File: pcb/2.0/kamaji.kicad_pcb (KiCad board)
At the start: 2 copper layers, 100 x 100 mm, 82 parts, among them J1 RJ10, J2 RJ10, J3 RJ10, J4 RJ10, J5 RJ10, J6 RJ10, J7 USB_B, J8 USB_A, Q1 2N3904, Q2 IRL540N, Q3 IRL540N, SW1 SW_Push, SW2 SW_Push, SW3 SW_Push, U1 ATMEGA32U4-AU, Y1 16MHz

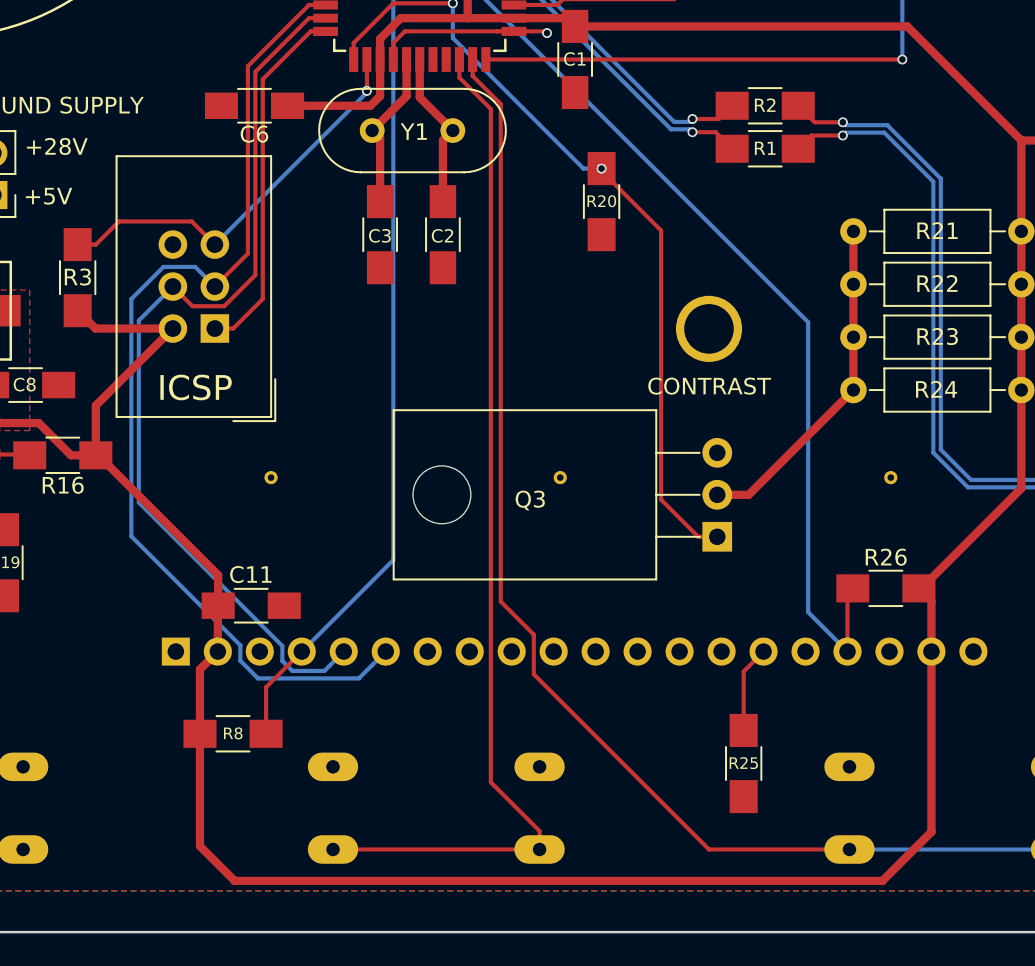
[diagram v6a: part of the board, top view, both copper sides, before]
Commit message: pull LCD_CS down
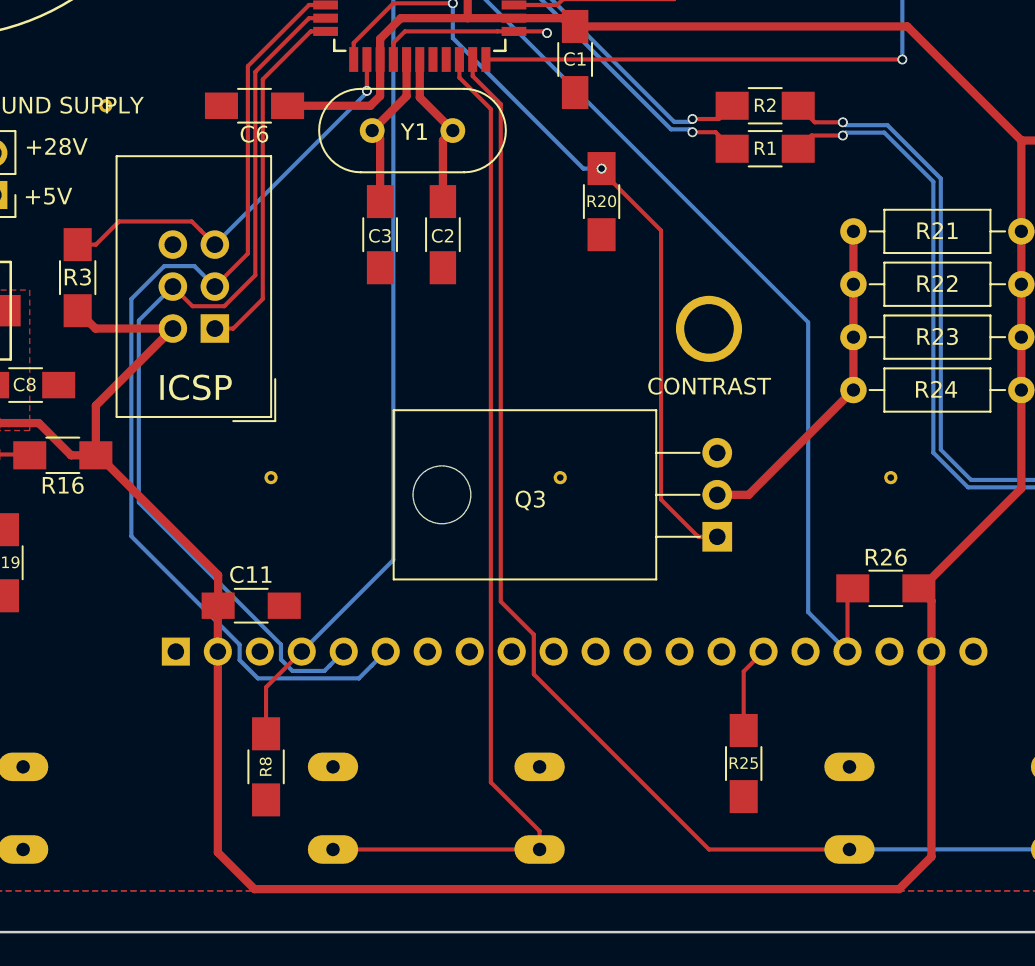
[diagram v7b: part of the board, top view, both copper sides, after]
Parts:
- added VIA**: Via_0.8mm, kamaji:Via_0.8mm, F.Cu at (80.0, 100.0)
- moved R8 2.83 mm to (89.7, 140.0), turned to 90 degrees
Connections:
- R8 pad 1: VCC -> GND
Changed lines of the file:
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@@
 (kicad_pcb (version 4) (host pcbnew 4.0.7)
   (general
-    (links 0)
-    (no_connects 0)
+    (links 178)
+    (no_connects 2)
     (area 49.924999 49.924999 150.075001 150.075001)
     (thickness 1.6)
     (drawings 16)
-    (tracks 380)
+    (tracks 378)
     (zones 0)
-    (modules 82)
+    (modules 83)
     (nets 57)
   )
@@
     (add_net VCC)
   )
+  (module kamaji:Via_0.8mm (layer F.Cu)
+    (at 80 100)
+    (fp_text reference VIA** (at 0 1.5) (layer F.SilkS) hide
+      (effects (font (size 1 1) (thickness 0.15)))
+    )
+    (fp_text value Via_0.8mm (at 0 -1.5) (layer F.Fab) hide
+      (effects (font (size 1 1) (thickness 0.15)))
+    )
+    (pad 1 thru_hole circle (at 0 0) (size 0.8 0.8) (drill 0.4) (layers *.Cu *.Mask)
+      (net 49 GND) (zone_connect 2))
+  )
   (module Connectors:1pin (layer F.Cu)
     (at 54 57)
@@
   )
   (module Resistors_SMD:R_1206_HandSoldering (layer F.Cu)
-    (at 87.7 138)
+    (at 89.7 140 90)
     (descr "Resistor SMD 1206, hand soldering")
     (tags "resistor 1206")
     (attr smd)
-    (fp_text reference R8 (at 0 0) (layer F.SilkS)
+    (fp_text reference R8 (at 0 0 90) (layer F.SilkS)
       (effects (font (size 0.7 0.7) (thickness 0.15)))
     )
-    (fp_text value 10K (at 0 1.9) (layer F.Fab)
-      (effects (font (size 1 1) (thickness 0.15)))
-    )
-    (fp_text user %R (at 0 0) (layer F.Fab)
+    (fp_text value 10K (at 0 1.9 90) (layer F.Fab)
+      (effects (font (size 1 1) (thickness 0.15)))
+    )
+    (fp_text user %R (at 0 0 90) (layer F.Fab)
       (effects (font (size 0.7 0.7) (thickness 0.105)))
     )
@@
     (fp_line (start 3.25 1.1) (end 3.25 -1.11) (layer F.CrtYd) (width 0.05))
     (fp_line (start 3.25 1.1) (end -3.25 1.1) (layer F.CrtYd) (width 0.05))
-    (pad 1 smd rect (at -2 0) (size 2 1.7) (layers F.Cu F.Paste F.Mask)
-      (net 3 VCC))
-    (pad 2 smd rect (at 2 0) (size 2 1.7) (layers F.Cu F.Paste F.Mask)
+    (pad 1 smd rect (at -2 0 90) (size 2 1.7) (layers F.Cu F.Paste F.Mask)
+      (net 49 GND))
+    (pad 2 smd rect (at 2 0 90) (size 2 1.7) (layers F.Cu F.Paste F.Mask)
       (net 7 /LCD_CS))
     (model ${KISYS3DMOD}/Resistors_SMD.3dshapes/R_1206.wrl
@@
   (segment (start 72.85 121.1) (end 75.35 121.1) (width 0.25) (layer F.Cu) (net 2))
   (segment (start 75.35 121.1) (end 75.4 121.15) (width 0.25) (layer F.Cu) (net 2))
+  (segment (start 129.961034 133.024284) (end 129.961034 145.438966) (width 0.5) (layer F.Cu) (net 3))
+  (segment (start 129.961034 145.438966) (end 128 147.4) (width 0.5) (layer F.Cu) (net 3))
+  (segment (start 89 147.4) (end 86.781034 145.181034) (width 0.5) (layer F.Cu) (net 3))
+  (segment (start 128 147.4) (end 89 147.4) (width 0.5) (layer F.Cu) (net 3))
+  (segment (start 86.781034 145.181034) (end 86.781034 133.024284) (width 0.5) (layer F.Cu) (net 3))
   (segment (start 96.6 88.05) (end 96.6 85.8) (width 0.5) (layer F.Cu) (net 3))
   (segment (start 96.6 88.05) (end 96.6 89.7) (width 0.5) (layer F.Cu) (net 3))
-  (segment (start 129.961034 133.024284) (end 129.961034 143.938966) (width 0.5) (layer F.Cu) (net 3))
-  (segment (start 129.961034 143.938966) (end 127 146.9) (width 0.5) (layer F.Cu) (net 3))
-  (segment (start 127 146.9) (end 87.8 146.9) (width 0.5) (layer F.Cu) (net 3))
-  (segment (start 85.7 144.8) (end 85.7 138) (width 0.5) (layer F.Cu) (net 3))
-  (segment (start 87.8 146.9) (end 85.7 144.8) (width 0.5) (layer F.Cu) (net 3))
   (segment (start 93.3 92.3) (end 94.55 92.3) (width 0.5) (layer F.Cu) (net 3))
   (segment (start 94.55 92.3) (end 96.6 90.25) (width 0.5) (layer F.Cu) (net 3))
@@
   (segment (start 86.781034 133.024284) (end 86.781034 130.268966) (width 0.5) (layer F.Cu) (net 3))
   (segment (start 86.781034 130.268966) (end 86.8 130.25) (width 0.5) (layer F.Cu) (net 3))
-  (segment (start 85.7 138) (end 85.7 134.105318) (width 0.5) (layer F.Cu) (net 3))
-  (segment (start 85.7 134.105318) (end 86.781034 133.024284) (width 0.5) (layer F.Cu) (net 3))
   (segment (start 135.4 117.2) (end 135.4 123.15) (width 0.5) (layer F.Cu) (net 3))
   (segment (start 129.35 129.2) (end 129.2 129.2) (width 0.5) (layer F.Cu) (net 3))
@@
   (segment (start 91.861034 133.024284) (end 89.7 135.185318) (width 0.25) (layer F.Cu) (net 7))
   (segment (start 89.7 135.185318) (end 89.7 138) (width 0.25) (layer F.Cu) (net 7))
+  (segment (start 84.06 110.94) (end 82.000022 112.999978) (width 0.25) (layer B.Cu) (net 8))
+  (segment (start 82.000022 112.999978) (end 82.000022 124.000022) (width 0.25) (layer B.Cu) (net 8))
+  (segment (start 82.000022 124.000022) (end 90.6 132.6) (width 0.25) (layer B.Cu) (net 8))
+  (segment (start 90.6 132.6) (end 90.6 133.502252) (width 0.25) (layer B.Cu) (net 8))
+  (segment (start 90.6 133.502252) (end 91.297032 134.199284) (width 0.25) (layer B.Cu) (net 8))
+  (segment (start 91.297032 134.199284) (end 93.226034 134.199284) (width 0.25) (layer B.Cu) (net 8))
+  (segment (start 93.226034 134.199284) (end 93.551035 133.874283) (width 0.25) (layer B.Cu) (net 8))
   (segment (start 93.551035 133.874283) (end 94.401034 133.024284) (width 0.25) (layer B.Cu) (net 8))
-  (segment (start 93.226034 134.199284) (end 93.551035 133.874283) (width 0.25) (layer B.Cu) (net 8))
-  (segment (start 90.686033 132.686033) (end 90.686033 133.588285) (width 0.25) (layer B.Cu) (net 8))
-  (segment (start 90.686033 133.588285) (end 91.297032 134.199284) (width 0.25) (layer B.Cu) (net 8))
-  (segment (start 91.297032 134.199284) (end 93.226034 134.199284) (width 0.25) (layer B.Cu) (net 8))
-  (segment (start 84.06 110.94) (end 82.000022 112.999978) (width 0.25) (layer B.Cu) (net 8))
-  (segment (start 82.000022 124.000022) (end 90.686033 132.686033) (width 0.25) (layer B.Cu) (net 8))
-  (segment (start 82.000022 112.999978) (end 82.000022 124.000022) (width 0.25) (layer B.Cu) (net 8))
   (segment (start 87.170529 112.128601) (end 89.049989 110.249141) (width 0.25) (layer F.Cu) (net 8))
   (segment (start 85.248601 112.128601) (end 87.170529 112.128601) (width 0.25) (layer F.Cu) (net 8))
@@
   (segment (start 89.049989 97.950011) (end 92.3 94.7) (width 0.25) (layer F.Cu) (net 8))
   (segment (start 89.049989 110.249141) (end 89.049989 97.950011) (width 0.25) (layer F.Cu) (net 8))
+  (segment (start 86.6 110.94) (end 85.36 109.7) (width 0.25) (layer B.Cu) (net 9))
+  (segment (start 85.36 109.7) (end 83.54087 109.7) (width 0.25) (layer B.Cu) (net 9))
+  (segment (start 81.550011 111.690859) (end 81.550011 126.054259) (width 0.25) (layer B.Cu) (net 9))
+  (segment (start 81.550011 126.054259) (end 88.1 132.604248) (width 0.25) (layer B.Cu) (net 9))
+  (segment (start 88.1 133.542252) (end 89.207043 134.649295) (width 0.25) (layer B.Cu) (net 9))
+  (segment (start 89.207043 134.649295) (end 95.316023 134.649295) (width 0.25) (layer B.Cu) (net 9))
   (segment (start 96.091035 133.874283) (end 96.941034 133.024284) (width 0.25) (layer B.Cu) (net 9))
-  (segment (start 88.146033 133.588285) (end 89.207043 134.649295) (width 0.25) (layer B.Cu) (net 9))
-  (segment (start 83.489471 109.751399) (end 81.550011 111.690859) (width 0.25) (layer B.Cu) (net 9))
-  (segment (start 88.146033 132.650281) (end 88.146033 133.588285) (width 0.25) (layer B.Cu) (net 9))
-  (segment (start 81.550011 111.690859) (end 81.550011 126.054259) (width 0.25) (layer B.Cu) (net 9))
-  (segment (start 81.550011 126.054259) (end 88.146033 132.650281) (width 0.25) (layer B.Cu) (net 9))
-  (segment (start 89.207043 134.649295) (end 95.316023 134.649295) (width 0.25) (layer B.Cu) (net 9))
+  (segment (start 83.54087 109.7) (end 81.550011 111.690859) (width 0.25) (layer B.Cu) (net 9))
+  (segment (start 88.1 132.604248) (end 88.1 133.542252) (width 0.25) (layer B.Cu) (net 9))
   (segment (start 95.316023 134.649295) (end 96.091035 133.874283) (width 0.25) (layer B.Cu) (net 9))
-  (segment (start 85.411399 109.751399) (end 83.489471 109.751399) (width 0.25) (layer B.Cu) (net 9))
-  (segment (start 86.6 110.94) (end 85.411399 109.751399) (width 0.25) (layer B.Cu) (net 9))
   (segment (start 92.3 93.9) (end 93.3 93.9) (width 0.25) (layer F.Cu) (net 9))
   (segment (start 88.599978 97.600022) (end 92.3 93.9) (width 0.25) (layer F.Cu) (net 9))

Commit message: minor PCB changes
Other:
- board text added: "SOUND"
- board text removed: "SOUND SUPPLY"
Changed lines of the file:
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@@
   (general
     (links 178)
-    (no_connects 2)
-    (area 49.924999 49.924999 150.075001 150.075001)
+    (no_connects 0)
+    (area 46.224999 46.55 157.775001 150.075001)
     (thickness 1.6)
     (drawings 16)
@@
     (pad_drill 3.048)
     (pad_to_mask_clearance 0.2)
-    (aux_axis_origin 0 0)
+    (aux_axis_origin 50 50)
     (visible_elements FFFFEF7F)
     (pcbplotparams
-      (layerselection 0x00030_80000001)
-      (usegerberextensions false)
+      (layerselection 0x010f0_80000001)
+      (usegerberextensions true)
       (excludeedgelayer true)
       (linewidth 0.100000)
@@
       (viasonmask false)
       (mode 1)
-      (useauxorigin false)
+      (useauxorigin true)
       (hpglpennumber 1)
       (hpglpenspeed 20)
@@
       (plotinvisibletext false)
       (padsonsilk false)
-      (subtractmaskfromsilk false)
+      (subtractmaskfromsilk true)
       (outputformat 1)
       (mirror false)
-      (drillshape 1)
+      (drillshape 0)
       (scaleselection 1)
-      (outputdirectory ""))
+      (outputdirectory gerbers/))
   )
   (net 0 "")
@@
     (descr "TO-220-3, Horizontal, RM 2.54mm")
     (tags "TO-220-3 Horizontal RM 2.54mm")
-    (fp_text reference Q2 (at 2.75 -10.5 90) (layer F.SilkS)
+    (fp_text reference Q2 (at 2.75 -11.2 180) (layer F.SilkS)
       (effects (font (size 1 1) (thickness 0.15)))
     )
@@
     (tags "resistor 1206")
     (attr smd)
-    (fp_text reference R8 (at 0 0 90) (layer F.SilkS)
+    (fp_text reference R8 (at 0 0 180) (layer F.SilkS)
       (effects (font (size 0.7 0.7) (thickness 0.15)))
     )
@@
     (tags "resistor 1206")
     (attr smd)
-    (fp_text reference R15 (at 0 -1.85 180) (layer F.SilkS)
+    (fp_text reference R15 (at 0 -2.2 180) (layer F.SilkS)
       (effects (font (size 1 1) (thickness 0.15)))
     )
@@
     (descr "SW PUSH 12mm https://www.e-switch.com/system/asset/product_line/data_sheet/143/TL1100.pdf")
     (tags "tact sw push 12mm")
-    (fp_text reference SW1 (at 2.54 2.366) (layer B.SilkS)
+    (fp_text reference SW1 (at 6.3 -2.4) (layer B.SilkS)
       (effects (font (size 1 1) (thickness 0.15)) (justify mirror))
     )
@@
     (descr "SW PUSH 12mm https://www.e-switch.com/system/asset/product_line/data_sheet/143/TL1100.pdf")
     (tags "tact sw push 12mm")
-    (fp_text reference SW2 (at 2.34 2.62) (layer B.SilkS)
+    (fp_text reference SW2 (at 6.45 -2.4) (layer B.SilkS)
       (effects (font (size 1 1) (thickness 0.15)) (justify mirror))
     )
@@
     (descr "SW PUSH 12mm https://www.e-switch.com/system/asset/product_line/data_sheet/143/TL1100.pdf")
     (tags "tact sw push 12mm")
-    (fp_text reference SW3 (at 2.594 2.54) (layer B.SilkS)
+    (fp_text reference SW3 (at 6.4 -2.4) (layer B.SilkS)
       (effects (font (size 1 1) (thickness 0.15)) (justify mirror))
     )
@@
     (descr "USB B connector")
     (tags "USB_B USB_DEV")
-    (fp_text reference J7 (at 1 5 180) (layer F.SilkS)
+    (fp_text reference J7 (at 5.1 1.07 180) (layer F.SilkS)
       (effects (font (size 1 1) (thickness 0.15)))
     )
@@
     (descr "USB A connector")
     (tags "USB USB_A")
-    (fp_text reference J8 (at 0 -2.35 90) (layer F.SilkS)
+    (fp_text reference J8 (at 3.56 2.67 180) (layer F.SilkS)
       (effects (font (size 1 1) (thickness 0.15)))
     )
@@
   (module kamaji:Potentiometer_Wheel_16mm (layer F.Cu)
     (at 56 100.25 90)
-    (fp_text reference RV2 (at 0 0 90) (layer F.SilkS)
+    (fp_text reference RV2 (at 0.05 0.6 180) (layer F.SilkS)
       (effects (font (size 1 1) (thickness 0.15)))
     )
@@
     (effects (font (size 1 1) (thickness 0.2)))
   )
-  (gr_text "SOUND SUPPLY" (at 77 100) (layer F.SilkS)
+  (gr_text SOUND (at 77.6 101.2) (layer F.SilkS)
     (effects (font (size 1 1) (thickness 0.2)))
   )
@@
     (effects (font (size 1 1) (thickness 0.2)))
   )
-  (gr_text +28V (at 77 102.5) (layer F.SilkS)
+  (gr_text +28V (at 77 103.2) (layer F.SilkS)
     (effects (font (size 1 1) (thickness 0.2)))
   )
